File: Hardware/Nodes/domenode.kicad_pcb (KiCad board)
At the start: 2 copper layers, 100 x 70 mm, 84 parts, among them J1 MIC_JUMPER, J10 5V, J11 TOUCH, J12 24V, J13 CAN_BOARD, J15 RGB_SHIELD, J16 RGB_SHIELD, J17 GROVE/I2C, J18 ISP, J19 CAN_IN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

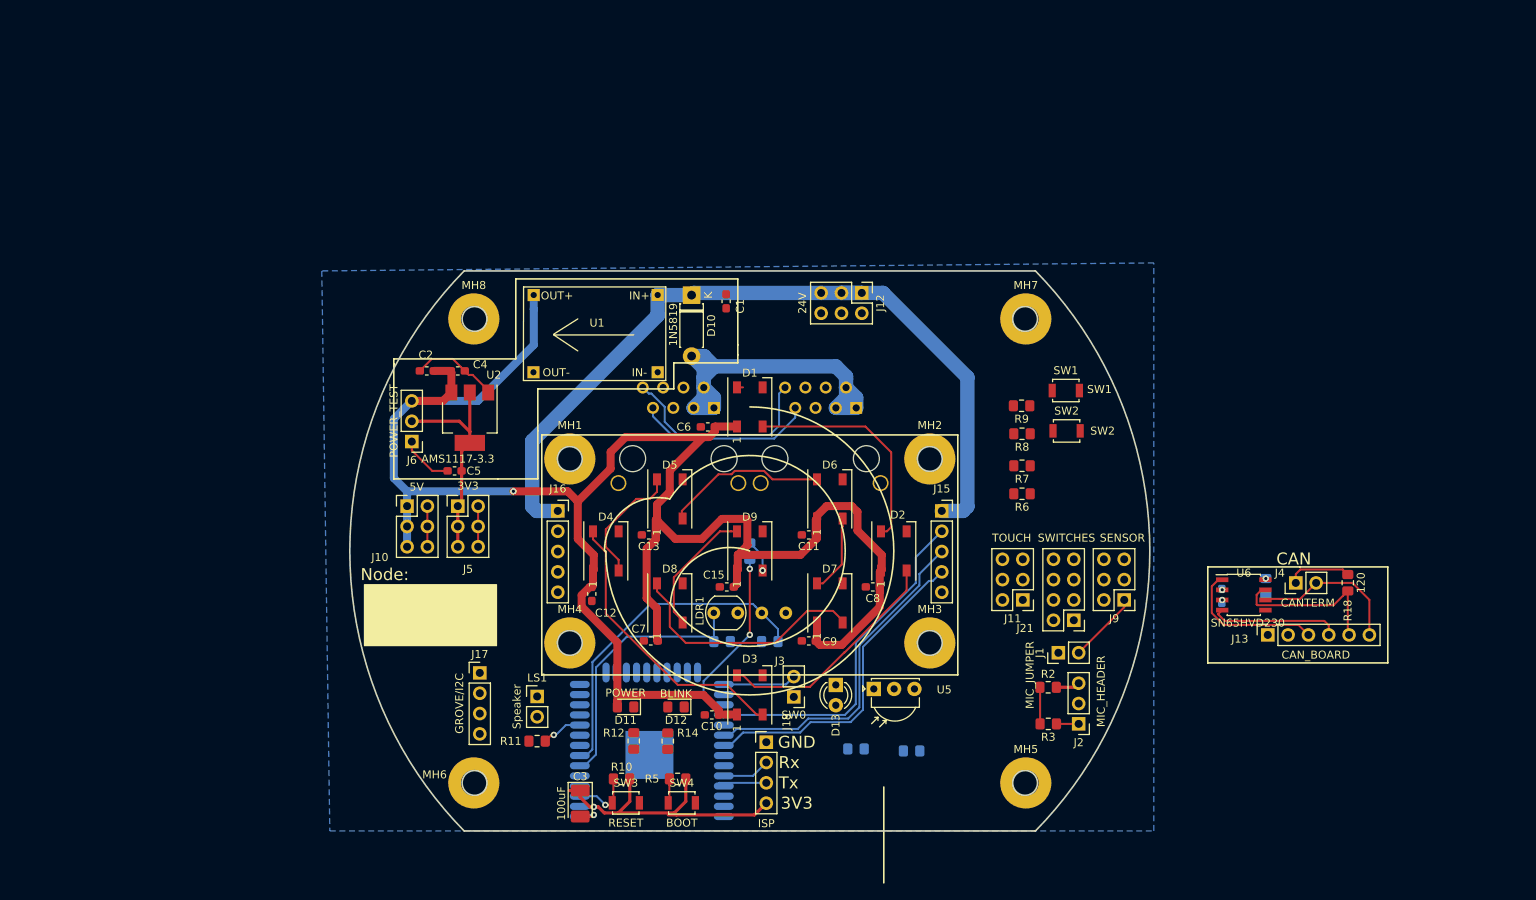
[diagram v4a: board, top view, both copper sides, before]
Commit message: wired up CAN L and H
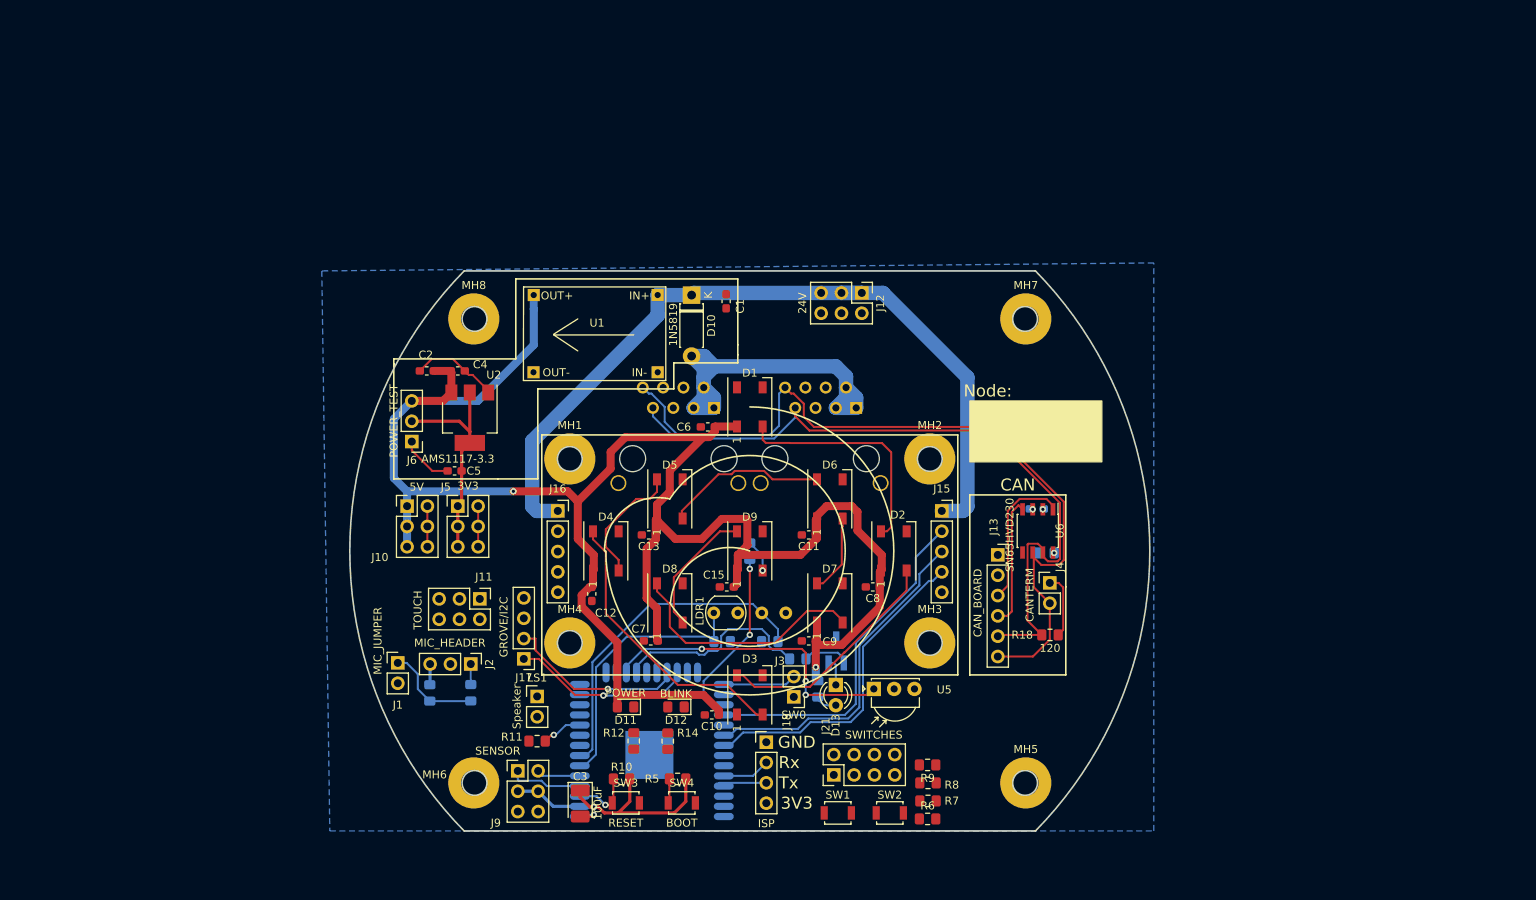
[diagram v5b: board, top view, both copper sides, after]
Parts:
- added Q2: 2N2222, Package_TO_SOT_SMD:SOT-23_Handsoldering, B.Cu at (159.3, 117.5)
- R2, R3: moved to B.Cu
- moved J1 82.6 mm to (104.5, 119.0), turned to 0 degrees
- moved J9 78.8 mm to (119.5, 132.5), turned to 0 degrees
- moved R2 77.3 mm to (108.5, 122.8), turned to 90 degrees
- moved J2 76.4 mm to (113.6, 119.1), turned to 270 degrees
- moved R3 72.3 mm to (113.6, 122.7), turned to 270 degrees
- moved J11 67.9 mm to (114.8, 111.0), turned to 270 degrees
- moved SW1 60.0 mm to (159.5, 137.8)
- moved SW2 52.6 mm to (166.0, 137.8)
- moved R9 46.4 mm to (170.7, 131.8)
- moved R8 45.2 mm to (170.8, 134.0)
- moved R7 43.5 mm to (170.8, 136.2)
- moved R6 42.3 mm to (170.7, 138.5), turned to 0 degrees
- moved R18 37.8 mm to (186.0, 115.5), turned to 0 degrees
- moved J21 35.7 mm to (159.0, 133.0), turned to 90 degrees
- moved J13 35.2 mm to (179.5, 105.5), turned to 0 degrees
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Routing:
- net CANL: track 45.3 -> 98.9 mm
- net CANH: track 42.6 -> 91.2 mm
- net IR_RX: track 0.00 -> 38.4 mm, vias 0 -> 3
- net IR_TX: track 0.00 -> 25.2 mm
- net SCL: track 0.00 -> 22.7 mm, vias 0 -> 1
- net SDA: track 0.00 -> 22.7 mm, vias 0 -> 1
- net Net-(J1-Pad1): track 4.58 -> 12.2 mm
- net Net-(Q2-Pad1): track 0.00 -> 5.90 mm
- net VCC: track 70.8 -> 65.1 mm
- net VN: track 0.00 -> 5.47 mm
- net Net-(D13-Pad1): track 0.00 -> 3.50 mm
- net +5V: track 245.1 -> 248.4 mm, vias 1 -> 2
- net Net-(D13-Pad2): track 0.00 -> 2.92 mm
- net Net-(D1-Pad2): track 28.3 -> 29.2 mm
- net Net-(D1-Pad4): track 0.75 -> 0.00 mm

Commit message: More PCBing
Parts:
- added Q1: MMBT918 (2N706 equiv), Package_TO_SOT_SMD:SOT-23_Handsoldering, B.Cu at (117.5, 120.8)
- Q2: value 2N2222 -> MMBT2222A (2N2222 equiv)
- moved D11 4.26 mm to (133.2, 120.2)
- moved D12 4.26 mm to (139.5, 120.2)
- moved Q2 0.25 mm to (159.2, 117.8), turned to 270 degrees
- moved R6 0.05 mm to (170.8, 138.5), turned to 180 degrees
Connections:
- Q2 pad 2: Net-(D13-Pad1) -> CANGND
- Q2 pad 3: CANGND -> Net-(D13-Pad1)
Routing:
- net CANGND: track 32.0 -> 84.3 mm, vias 2 -> 4
- net SW4: track 0.00 -> 50.3 mm, vias 0 -> 1
- net CRX: track 16.4 -> 63.8 mm, vias 0 -> 2
- net CTX: track 18.2 -> 65.5 mm, vias 0 -> 2
- net SW3: track 0.00 -> 46.5 mm, vias 0 -> 2
- net TOUCH3: track 0.00 -> 41.8 mm, vias 0 -> 2
- net SW1: track 0.00 -> 32.4 mm, vias 0 -> 1
- net SW2: track 0.00 -> 31.0 mm
- net +5V: track 248.4 -> 273.8 mm
- net VCC: track 65.1 -> 85.0 mm
- net TOUCH5: track 0.00 -> 19.8 mm
- net SW0: track 14.0 -> 30.3 mm, vias 0 -> 3
- net Net-(Q1-Pad1): track 0.00 -> 8.25 mm, vias 0 -> 1
- net Net-(LS1-Pad1): track 0.00 -> 6.31 mm
- net Net-(Q2-Pad1): track 5.90 -> 4.41 mm
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- added copper zone on F.Cu, net CANGND
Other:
- net class CAN+ added: clearance 0.2, trace_width 0.25, via_dia 0.8, via_drill 0.4
- net class CAN- added: clearance 0.2, trace_width 0.25, via_dia 0.8, via_drill 0.4

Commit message: Almost done!
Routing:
- net VCC: track 85.0 -> 95.6 mm
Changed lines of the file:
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@@
     (thickness 1.6)
     (drawings 52)
-    (tracks 642)
+    (tracks 644)
     (zones 0)
     (modules 86)
@@
   (segment (start 132.070001 137.750001) (end 138.75 137.750001) (width 0.4) (layer F.Cu) (net 5))
   (segment (start 138.75 137.750001) (end 139.070001 137.750001) (width 0.4) (layer F.Cu) (net 5))
+  (segment (start 171.75 124.92) (end 171.75 131.75) (width 0.4) (layer F.Cu) (net 5))
+  (segment (start 169.08 122.25) (end 171.75 124.92) (width 0.4) (layer F.Cu) (net 5))
   (segment (start 170.88641 108.75) (end 171.37 108.75) (width 0.25) (layer B.Cu) (net 6))
   (segment (start 162.65002 116.98639) (end 170.88641 108.75) (width 0.25) (layer B.Cu) (net 6))

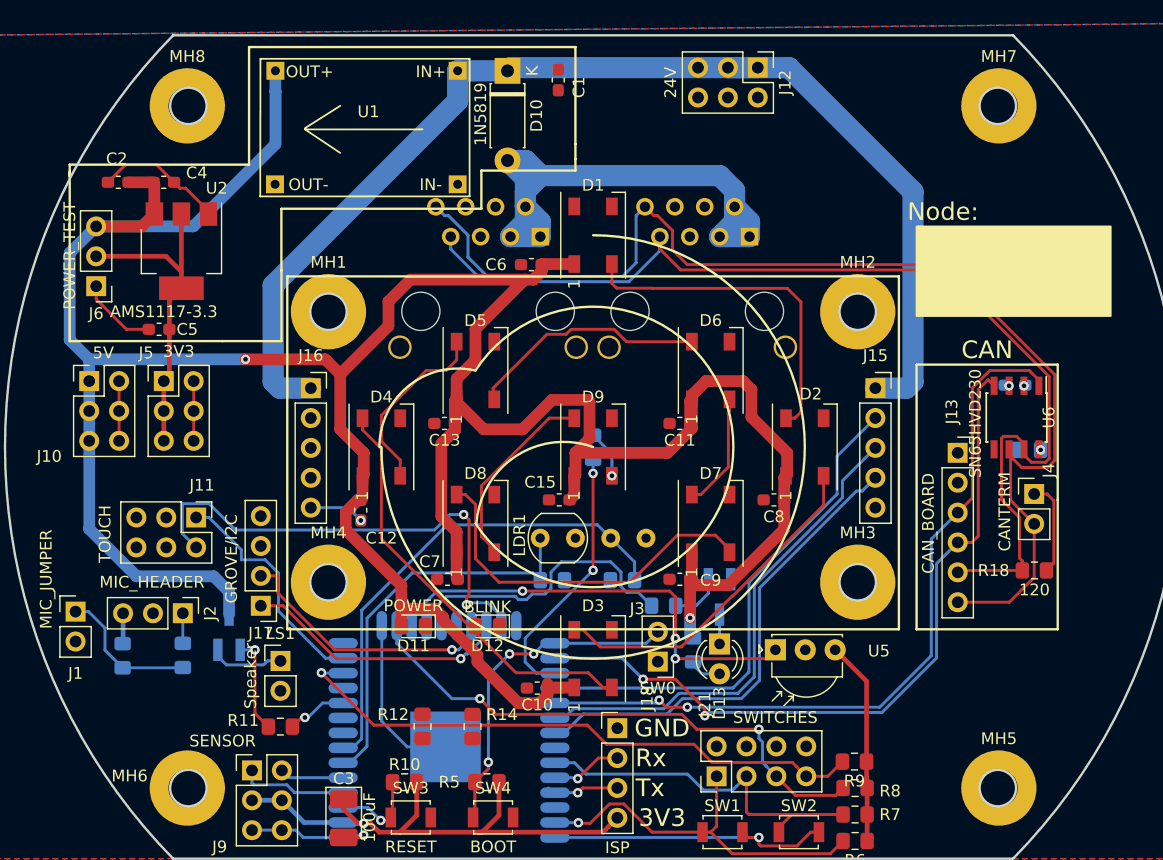
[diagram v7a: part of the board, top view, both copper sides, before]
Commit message: Fixed capacitive pads and traced them out
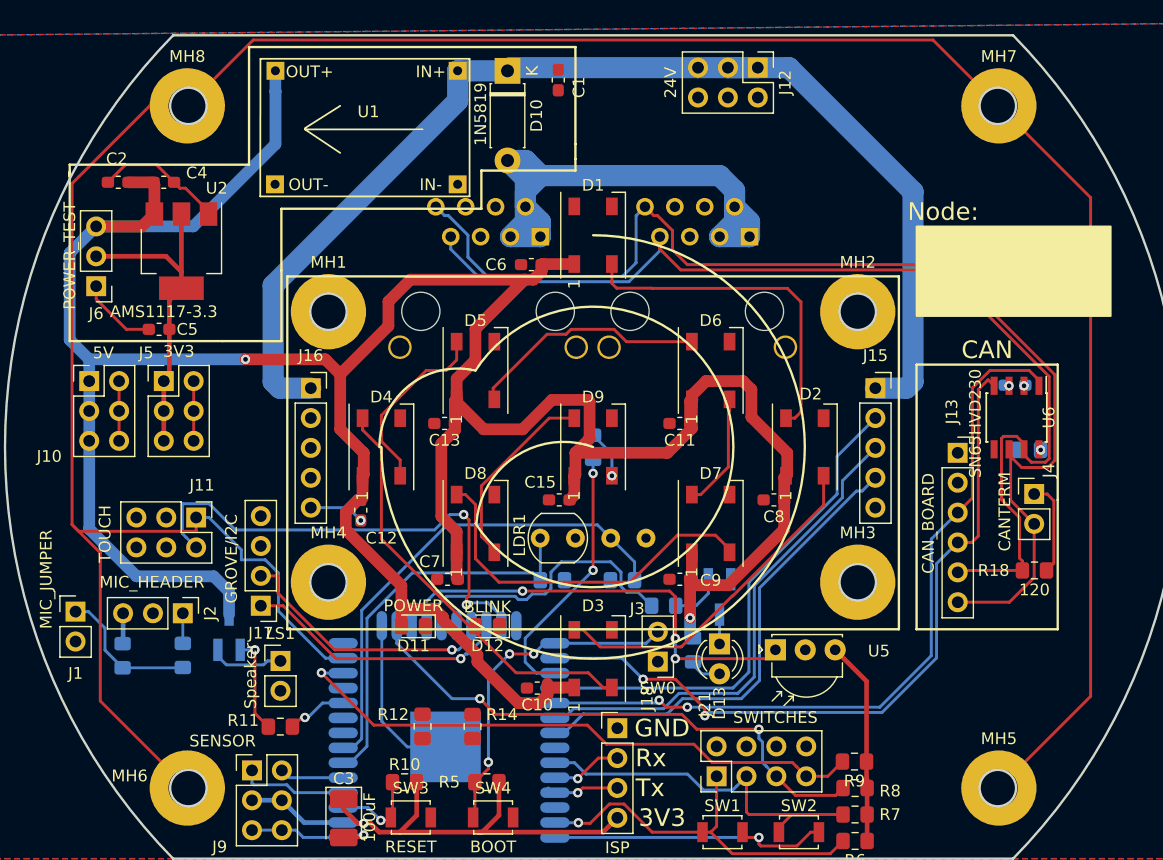
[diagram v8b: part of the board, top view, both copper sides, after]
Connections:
- MH6 pad 1: Net-(MH6-Pad1) -> TOUCH5
- MH8 pad 1: Net-(MH6-Pad1) -> TOUCH5
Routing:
- net TOUCH5: track 19.8 -> 237.9 mm
